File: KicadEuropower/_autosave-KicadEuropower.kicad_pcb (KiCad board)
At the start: 2 copper layers, 100 x 100 mm, 109 parts, among them J1 Conn_01x02_Male, J2 Conn_01x02_Male, J3 Conn_01x02_Male, J4 Conn_01x03_Male, J5 Conn_01x03_Male, J6 Conn_01x03_Male, P1 Doepfer_Power_10pin, P10 Doepfer_Power_10pin, P11 Doepfer_Power_10pin, P12 Doepfer_Power_10pin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

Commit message: DRC ok
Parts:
- TP1: value TestPoint -> VGnd
- moved C9 3.77 mm to (85.2, 2.75)
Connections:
- P1 pad 10: Net-(P1-Pad10) -> +12V
- P1 pad 9: Net-(P1-Pad10) -> +12V
- P2 pad 9: Net-(P1-Pad10) -> +12V
- P3 pad 10: Net-(P3-Pad10) -> +12V
- P3 pad 9: Net-(P3-Pad10) -> +12V
- P4 pad 9: Net-(P3-Pad10) -> +12V
- P5 pad 10: Net-(P5-Pad10) -> +12V
- P5 pad 9: Net-(P5-Pad10) -> +12V
- P6 pad 9: Net-(P5-Pad10) -> +12V
- P7 pad 10: Net-(P7-Pad10) -> +12V
- P7 pad 9: Net-(P7-Pad10) -> +12V
- P8 pad 9: Net-(P7-Pad10) -> +12V
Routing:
- net +5V: track 0.00 -> 331.1 mm, vias 0 -> 4
- net +12V: track 0.00 -> 324.7 mm, vias 0 -> 5
- net -12V: track 116.1 -> 270.9 mm, vias 0 -> 2
- net GND: track 13.1 -> 92.1 mm, vias 0 -> 4
- net CV: track 0.00 -> 71.5 mm
- net Gate: track 0.00 -> 69.1 mm
- net /+5V-ext: track 0.00 -> 33.7 mm
- net Net-(C3-Pad1): track 0.00 -> 31.0 mm, vias 0 -> 2
- net Net-(C10-Pad1): track 0.00 -> 21.6 mm
- net VinGND: track 0.00 -> 19.9 mm, vias 0 -> 2
- net /+15v-int: track 0.00 -> 17.0 mm
- net Net-(C2-Pad1): track 0.00 -> 16.8 mm
- net Net-(D2-Pad2): track 0.00 -> 15.8 mm
- net Vin-15: track 98.6 -> 111.3 mm
- net Net-(D8-Pad2): track 0.00 -> 5.72 mm, vias 0 -> 1
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
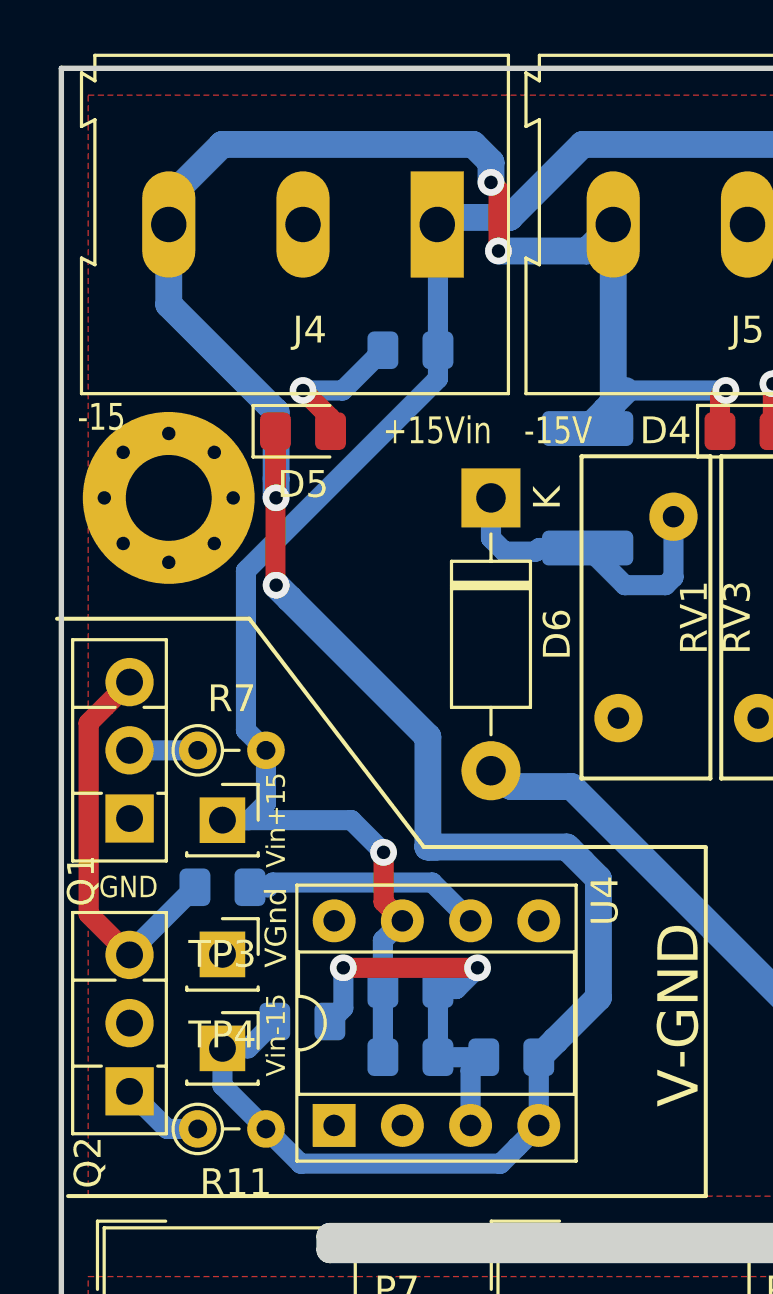
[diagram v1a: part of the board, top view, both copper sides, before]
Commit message: Cleared zones around mounting holes - 3D rendered img
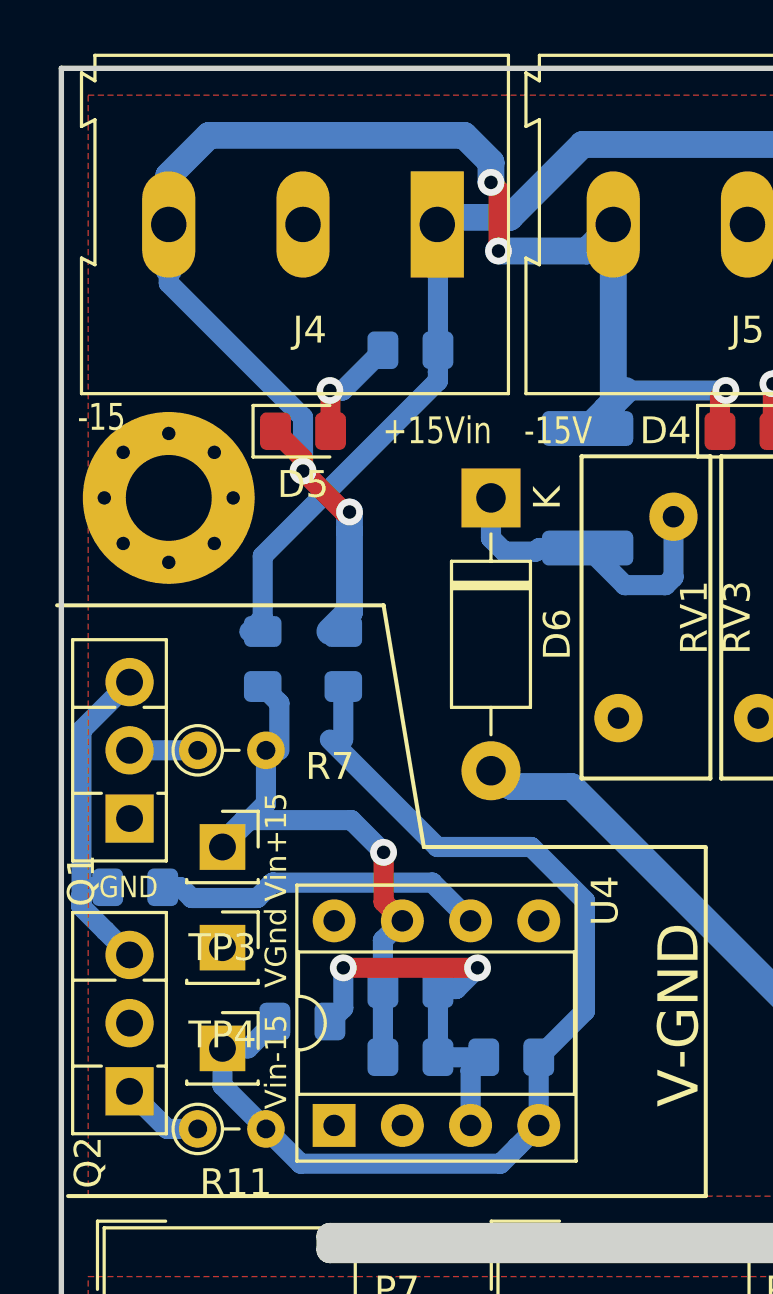
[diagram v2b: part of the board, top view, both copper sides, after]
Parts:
- added R12: 0R, Resistor_SMD:R_0805_2012Metric_Pad1.15x1.40mm_HandSolder, B.Cu at (7.50, 22.0)
- added R13: 0R, Resistor_SMD:R_0805_2012Metric_Pad1.15x1.40mm_HandSolder, B.Cu at (10.5, 22.0)
- moved R9 3.25 mm to (2.75, 30.5)
- moved TP2 1.00 mm to (6.00, 29.0)
- moved TP3 0.25 mm to (6.00, 32.8)
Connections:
- C45 pad 1: Vin+15 -> Net-(C45-Pad1)
- C46 pad 2: Vin-15 -> Net-(C46-Pad2)
- R10 pad 2: Vin-15 -> Net-(C46-Pad2)
- R11 pad 2: Vin-15 -> Net-(C46-Pad2)
- R7 pad 2: Vin+15 -> Net-(C45-Pad1)
- R8 pad 1: Vin+15 -> Net-(C45-Pad1)
- TP2 pad 1: Vin+15 -> Net-(C45-Pad1)
- TP4 pad 1: Vin-15 -> Net-(C46-Pad2)
- U4 pad 4: Vin-15 -> Net-(C46-Pad2)
- U4 pad 7: Vin+15 -> Net-(C45-Pad1)
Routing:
- net Vin-15: track 111.3 -> 61.5 mm
- net Net-(C46-Pad2): track 0.00 -> 40.4 mm
- net Vin+15: track 68.9 -> 46.6 mm, vias 1 -> 0
- net Net-(C45-Pad1): track 0.00 -> 21.9 mm, vias 0 -> 1
- net Net-(R9-Pad2): track 8.88 -> 12.7 mm
- net Net-(Q1-Pad3): track 15.0 -> 13.3 mm
- net Net-(D5-Pad2): track 5.54 -> 4.12 mm
